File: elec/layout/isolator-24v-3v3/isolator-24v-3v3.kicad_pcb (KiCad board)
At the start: 2 copper layers, 13 parts, among them U1 470nF ±20% 16V X5R, U10 2.75V, U11 1kΩ ±1% 62.5mW, U12 2.2µF ±10% 25V X7R, U2 1kΩ ±1% 62.5mW, U3 infΩ infW, U5 10µH ±20%, U6 2.2µF ±20% 6.3V X5R, U7 10µF ±10% 25V X5R, U9 2.2µF ±10% 25V X7R

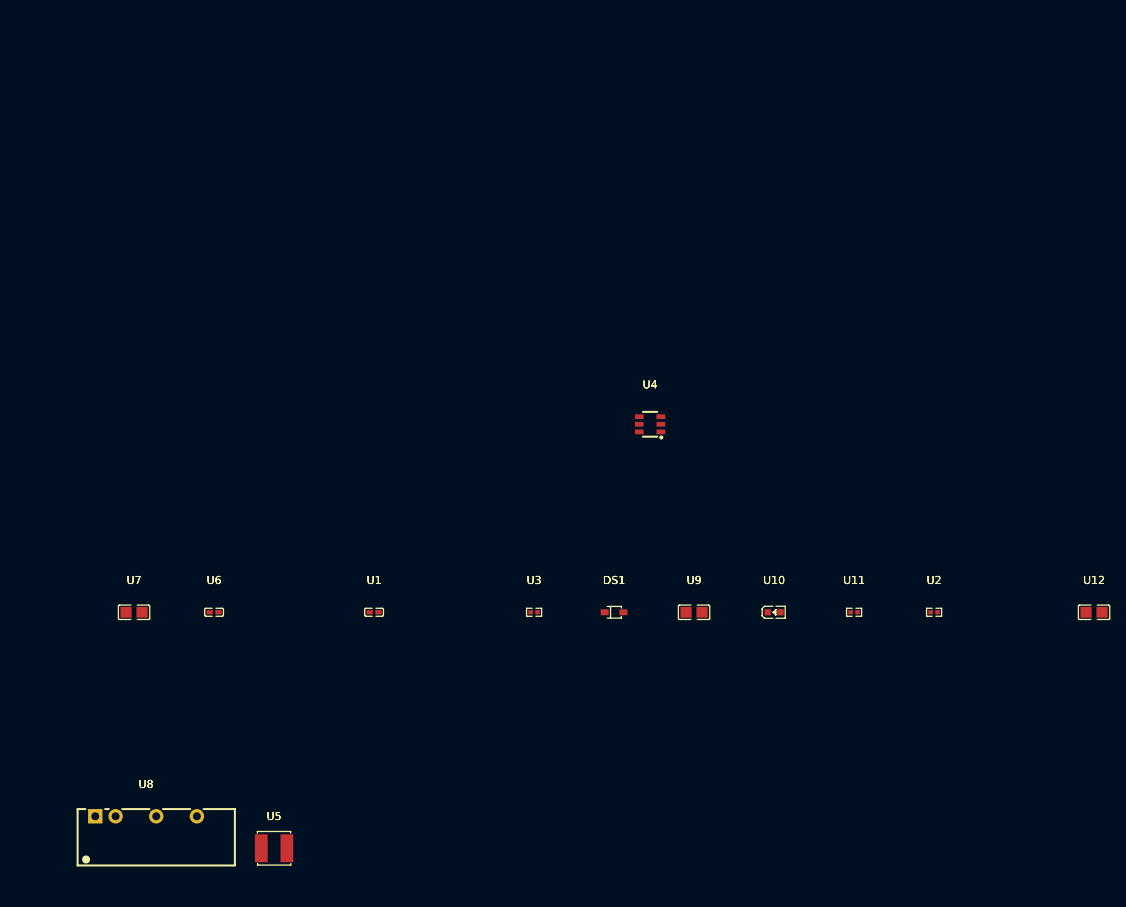
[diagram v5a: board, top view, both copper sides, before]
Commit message: update syntax, delete vendored packages
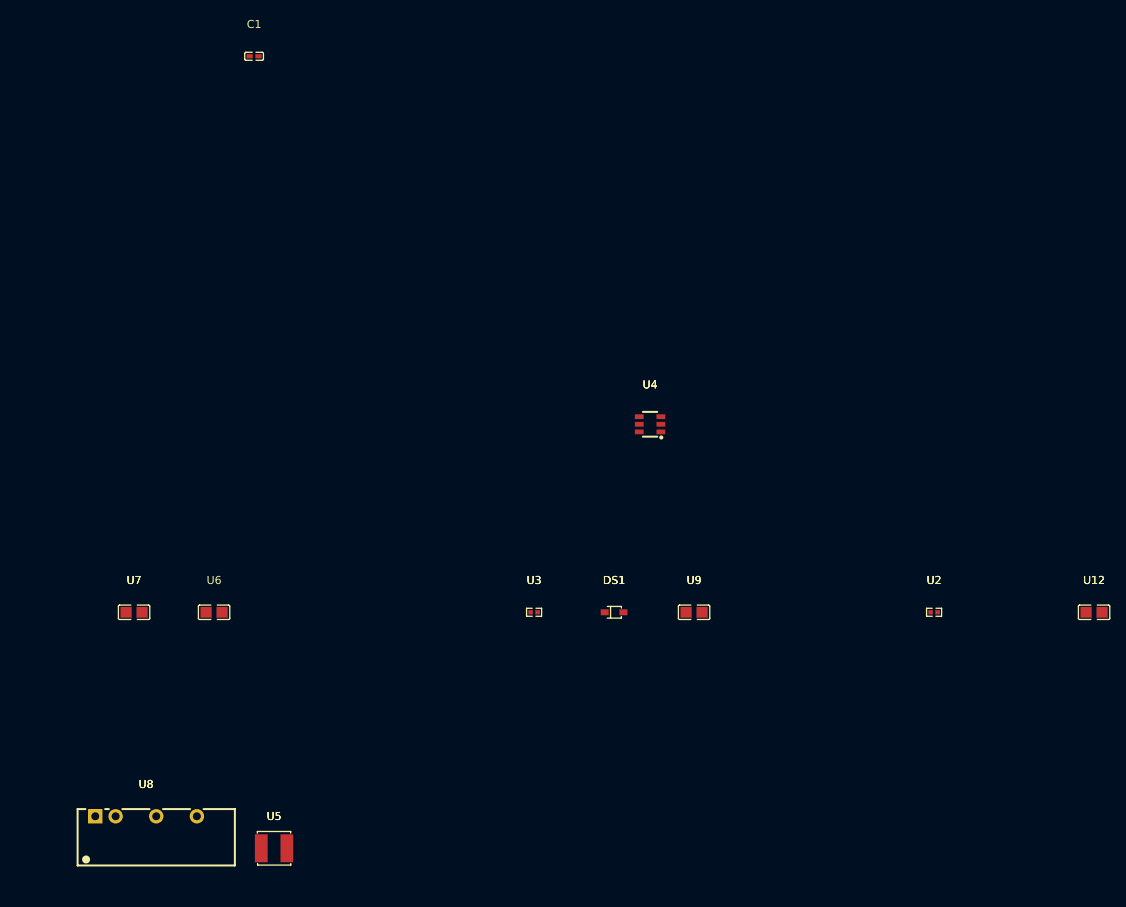
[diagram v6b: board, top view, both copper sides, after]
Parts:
- removed U1: 470nF ±20% 16V X5R, atopile:C0402-b3ef17
- removed U10: 2.75V, lib:LED0603-RD
- removed U11: 1kΩ ±1% 62.5mW, atopile:R0402-56259e
- added C1: 470nF ±20% 16V X5R, atopile:C0402-b3ef17, F.Cu at (100.0, -5.00)
- U2: value 1kΩ ±1% 62.5mW -> 8.2kΩ ±1% 62.5mW
- U3: value infΩ infW -> 10kΩ ±1% 62.5mW
- U6: value 2.2µF ±20% 6.3V X5R -> 10µF ±10% 25V X5R; footprint atopile:C0402-b3ef17 -> atopile:C0805-3b2e55
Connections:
- net out renamed line
- DS1 pad 2: gnd-1 -> gnd
- U12 pad 1: anode -> hv
- U12 pad 2: gnd -> gnd-2
- U2 pad 2: gnd-1 -> gnd
- U4 pad 2: gnd-1 -> gnd
- U4 pad 4: hv -> hv-2
- U4 pad 5: hv -> hv-2
- U6 pad 1: hv -> hv-2
- U6 pad 2: gnd-1 -> gnd
- U7 pad 2: gnd-1 -> gnd
- U8 pad 1: hv -> hv-2
- U8 pad 2: gnd-1 -> gnd
- U8 pad 4: gnd -> gnd-2
- U8 pad 6: anode -> hv
- U9 pad 1: hv -> hv-2
- U9 pad 2: gnd-1 -> gnd

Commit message: build and re-link layouts
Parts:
- added U1: 470nF ±20% 16V X5R, atopile:C0402-b3ef17, F.Cu at (75.3, 89.3)
- moved U12 117.1 mm to (90.1, 87.4), turned to 180 degrees
- moved C1 95.8 mm to (106.4, 90.6), turned to -90 degrees
- moved U2 90.1 mm to (100.2, 94.8), turned to -90 degrees
- moved U9 77.2 mm to (81.2, 87.2)
- moved U4 66.6 mm to (104.2, 89.8), turned to 90 degrees
- moved DS1 45.3 mm to (107.7, 90.1), turned to 90 degrees
- moved U3 44.9 mm to (100.2, 92.8), turned to -90 degrees
- moved U7 34.1 mm to (101.9, 94.1), turned to -90 degrees
- moved U6 26.1 mm to (101.4, 89.8), turned to 90 degrees
- moved U5 3.17 mm to (105.7, 94.3), turned to 180 degrees
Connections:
- U12 pad 1: hv -> hv-2
- U4 pad 4: hv-2 -> hv
- U4 pad 5: hv-2 -> hv
- U6 pad 1: hv-2 -> hv
- U8 pad 1: hv-2 -> hv
- U8 pad 6: hv -> hv-2
- U9 pad 1: hv-2 -> hv
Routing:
- net gnd: track 0.00 -> 10.0 mm, vias 0 -> 4
- net line: track 0.00 -> 9.13 mm, vias 0 -> 2
- net hv-2: track 0.00 -> 3.34 mm
- net gnd-2: track 0.00 -> 3.19 mm
- net hv: track 0.00 -> 2.88 mm
- net CB: track 0.00 -> 2.36 mm
- added copper zone on F.Cu, net cathode
- added copper zone on F.Cu, net hv
- added copper zone on F.Cu, net hv-1

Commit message: all modules building
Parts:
- removed U1: 470nF ±20% 16V X5R, atopile:C0402-b3ef17
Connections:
- DS1 pad 2: gnd -> gnd-1
- U12 pad 1: hv-2 -> hv-1
- U12 pad 2: gnd-2 -> gnd
- U2 pad 2: gnd -> gnd-1
- U3 pad 1: hv-1 -> hv-2
- U4 pad 4: hv -> hv-1
- U4 pad 5: hv -> hv-1
- U5 pad 2: hv-1 -> hv-2
- U6 pad 1: hv -> hv-1
- U7 pad 1: hv-1 -> hv-2
- U7 pad 2: gnd -> gnd-1
- U8 pad 2: gnd -> gnd-1
- U8 pad 4: gnd-2 -> gnd
- U8 pad 6: hv-2 -> hv-1
- U9 pad 2: gnd -> gnd-1
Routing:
- net gnd-1: track 0.00 -> 10.0 mm, vias 0 -> 4
- net gnd: track 10.0 -> 0.00 mm, vias 4 -> 0
- net (no net): track 0.00 -> 6.53 mm
- net hv-2: track 3.34 -> 0.00 mm
- net gnd-2: track 3.19 -> 0.00 mm
- added copper zone on F.Cu, net hv-2
- removed copper zone on F.Cu, net hv-1
